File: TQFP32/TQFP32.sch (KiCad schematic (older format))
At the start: 2 parts, among them J1 Conn_01x30, U1 ATmega8L-8AU

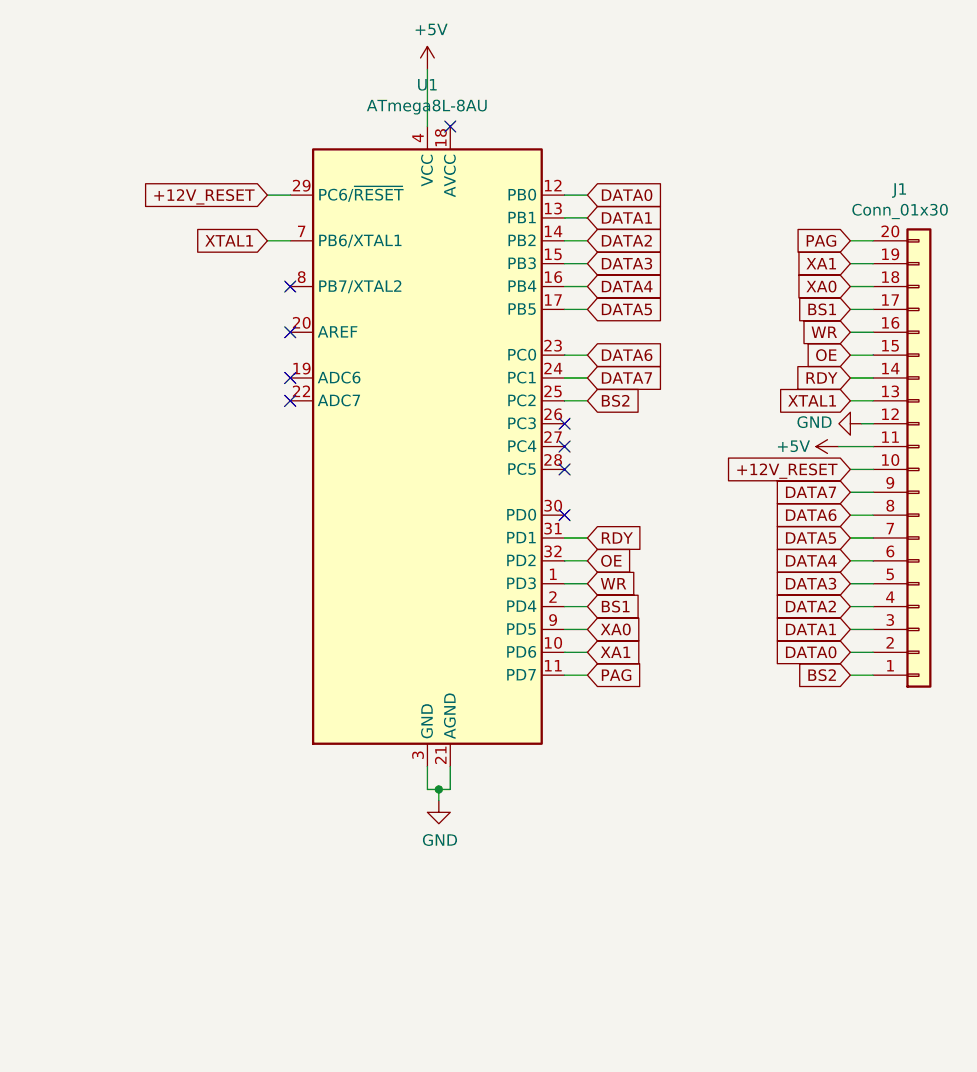
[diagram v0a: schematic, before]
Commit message: Added ISP6 & LED for RESET & LED for POWER
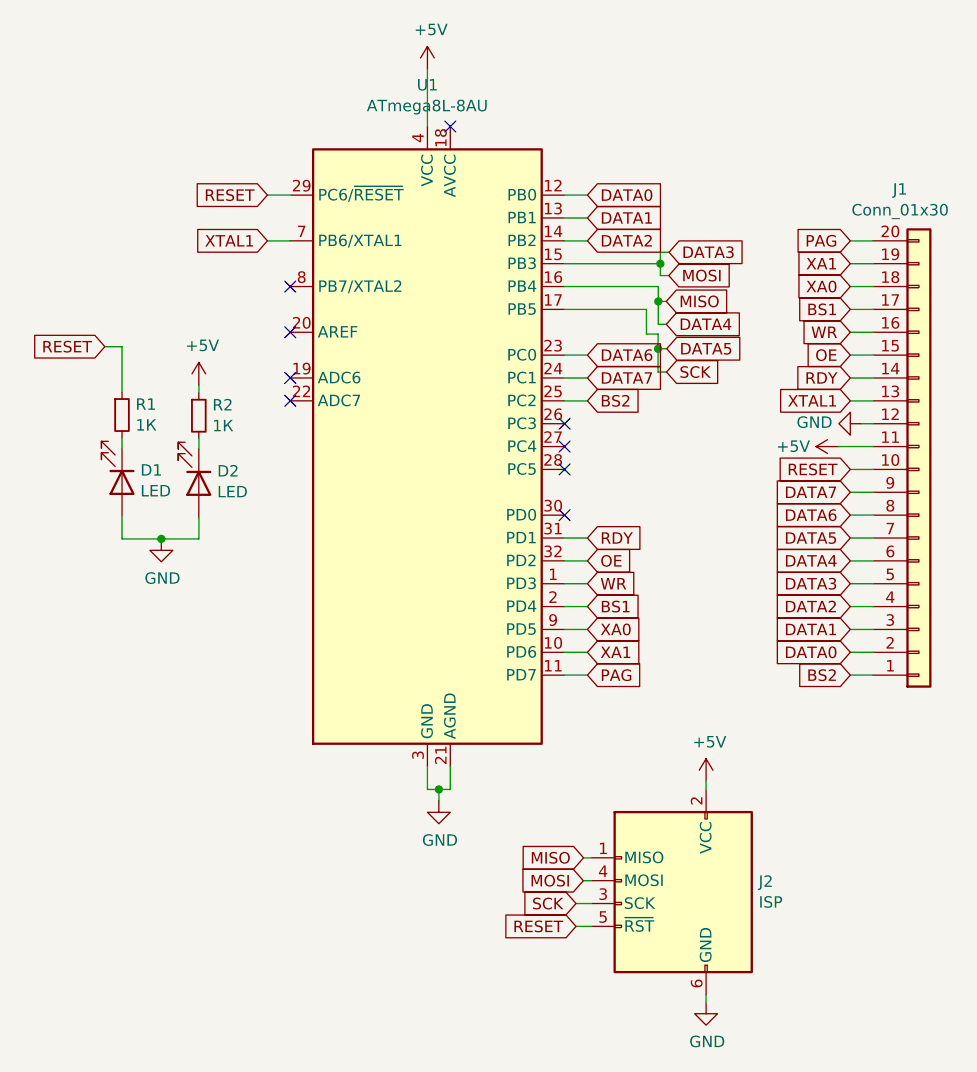
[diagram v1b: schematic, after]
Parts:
- added D1, D2: LED, LED_SMD:LED_0805_2012Metric_Pad1.15x1.40mm_HandSolder, symbol Device:LED
- added J2: ISP, Connector_PinHeader_2.54mm:PinHeader_2x03_P2.54mm_Vertical, symbol Connector:AVR-ISP-6
- added R1, R2: 1К, Resistor_SMD:R_0805_2012Metric_Pad1.20x1.40mm_HandSolder, symbol Device:R_Small
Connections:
- net +5V: now also J2.2 (VCC), R2.1
- net DATA3: now also J2.4 (MOSI)
- net DATA4: now also J2.1 (MISO)
- net DATA5: now also J2.3 (SCK)
- net GND: now also D1.2 (A), D2.2 (A), J2.6 (GND)
- net +12V_RESET renamed RESET
- net RESET: now also J2.5 (~RST), R1.1
- new net: D2.1 (K), R2.2
- new net: D1.1 (K), R1.2
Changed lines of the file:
@@
 $EndDescr
 Text GLabel 4300 2000 0    50   Input ~ 0
-+12V_RESET
+RESET
 Wire Wire Line
 	4300 2000 4400 2000
@@
 Wire Wire Line
 	5700 2100 5600 2100
-Text GLabel 5700 2200 2    50   Input ~ 0
-DATA2
 Wire Wire Line
 	5700 2200 5600 2200
-Wire Wire Line
-	5700 2300 5600 2300
-Text GLabel 5700 2300 2    50   Input ~ 0
-DATA3
-Text GLabel 5700 2400 2    50   Input ~ 0
-DATA4
-Text GLabel 5700 2500 2    50   Input ~ 0
-DATA5
-Wire Wire Line
-	5600 2400 5700 2400
-Wire Wire Line
-	5600 2500 5700 2500
 Text GLabel 5700 2700 2    50   Input ~ 0
 DATA6
@@
 	6950 2200 6850 2200
 Text GLabel 6850 3200 0    50   Input ~ 0
-+12V_RESET
+RESET
 Wire Wire Line
 	6850 3200 6950 3200
@@
 Wire Wire Line
 	6900 3000 6950 3000
+$Comp
+L Connector:AVR-ISP-6 J2
+U 1 1 60AF4D40
+P 6119 5099
+F 0 "J2" H 5789 5195 50  0000 R CNN
+F 1 "ISP" H 5789 5104 50  0000 R CNN
+F 2 "Connector_PinHeader_2.54mm:PinHeader_2x03_P2.54mm_Vertical" V 5869 5149 50  0001 C CNN
+F 3 " ~" H 4844 4549 50  0001 C CNN
+	1    6119 5099
+	-1   0    0    -1
+$EndComp
+Text GLabel 6045 2565 2    50   Input ~ 0
+DATA4
+Wire Wire Line
+	5600 2400 6010 2400
+Text GLabel 6045 2465 2    50   Input ~ 0
+MISO
+Text GLabel 6056 2352 2    50   Input ~ 0
+MOSI
+Text GLabel 5700 2200 2    50   Input ~ 0
+DATA2
+Wire Wire Line
+	6045 2465 6010 2465
+Wire Wire Line
+	6010 2465 6010 2400
+Wire Wire Line
+	6010 2465 6010 2565
+Wire Wire Line
+	6010 2565 6045 2565
+Connection ~ 6010 2465
+Text GLabel 6057 2250 2    50   Input ~ 0
+DATA3
+Wire Wire Line
+	6019 2300 6019 2250
+Wire Wire Line
+	6019 2250 6057 2250
+Wire Wire Line
+	5600 2300 6019 2300
+Wire Wire Line
+	6056 2352 6019 2352
+Wire Wire Line
+	6019 2352 6019 2300
+Connection ~ 6019 2300
+Text GLabel 6046 2774 2    50   Input ~ 0
+SCK
+Text GLabel 6047 2672 2    50   Input ~ 0
+DATA5
+Wire Wire Line
+	6046 2774 6009 2774
+Wire Wire Line
+	6009 2672 6047 2672
+Wire Wire Line
+	5958 2500 5958 2608
+Wire Wire Line
+	5958 2608 6009 2608
+Wire Wire Line
+	5600 2500 5958 2500
+Wire Wire Line
+	6009 2608 6009 2672
+Connection ~ 6009 2672
+Wire Wire Line
+	6009 2672 6009 2774
+Text GLabel 5683 4899 0    50   Input ~ 0
+MISO
+Text GLabel 5682 4999 0    50   Input ~ 0
+MOSI
+Text GLabel 5650 5099 0    50   Input ~ 0
+SCK
+Wire Wire Line
+	5719 5099 5650 5099
+Wire Wire Line
+	5683 4899 5719 4899
+Wire Wire Line
+	5719 4999 5682 4999
+Text GLabel 5650 5199 0    50   Input ~ 0
+RESET
+Wire Wire Line
+	5719 5199 5650 5199
+$Comp
+L power:GND #PWR0105
+U 1 1 60B56BC6
+P 6219 5531
+F 0 "#PWR0105" H 6219 5281 50  0001 C CNN
+F 1 "GND" H 6224 5358 50  0000 C CNN
+F 2 "" H 6219 5531 50  0001 C CNN
+F 3 "" H 6219 5531 50  0001 C CNN
+	1    6219 5531
+	1    0    0    -1
+$EndComp
+$Comp
+L power:+5V #PWR0106
+U 1 1 60B574EF
+P 6219 4566
+F 0 "#PWR0106" H 6219 4416 50  0001 C CNN
+F 1 "+5V" H 6234 4739 50  0000 C CNN
+F 2 "" H 6219 4566 50  0001 C CNN
+F 3 "" H 6219 4566 50  0001 C CNN
+	1    6219 4566
+	1    0    0    -1
+$EndComp
+Wire Wire Line
+	6219 4566 6219 4599
+Wire Wire Line
+	6219 5531 6219 5499
+$Comp
+L Device:LED D2
+U 1 1 60B87E9D
+P 4000 3261
+F 0 "D2" V 3947 3341 50  0000 L CNN
+F 1 "LED" V 4038 3341 50  0000 L CNN
+F 2 "LED_SMD:LED_0805_2012Metric_Pad1.15x1.40mm_HandSolder" H 4000 3261 50  0001 C CNN
+F 3 "~" H 4000 3261 50  0001 C CNN
+	1    4000 3261
+	0    1    1    0
+$EndComp
+$Comp
+L Device:LED D1
+U 1 1 60B8D8E2
+P 3664 3257
+F 0 "D1" V 3611 3337 50  0000 L CNN
+F 1 "LED" V 3702 3337 50  0000 L CNN
+F 2 "LED_SMD:LED_0805_2012Metric_Pad1.15x1.40mm_HandSolder" H 3664 3257 50  0001 C CNN
+F 3 "~" H 3664 3257 50  0001 C CNN
+	1    3664 3257
+	0    1    1    0
+$EndComp
+$Comp
+L power:GND #PWR0107
+U 1 1 60B93CD4
+P 3836 3504
+F 0 "#PWR0107" H 3836 3254 50  0001 C CNN
+F 1 "GND" H 3841 3331 50  0000 C CNN
+F 2 "" H 3836 3504 50  0001 C CNN
+F 3 "" H 3836 3504 50  0001 C CNN
+	1    3836 3504
+	1    0    0    -1
+$EndComp
+Wire Wire Line
+	3664 3407 3664 3504
+Wire Wire Line
+	3664 3504 3836 3504
+Wire Wire Line
+	3836 3504 4000 3504
+Wire Wire Line
+	4000 3504 4000 3411
+Connection ~ 3836 3504
+Text GLabel 3589 2663 0    50   Input ~ 0
+RESET
+$Comp
+L Device:R_Small R2
+U 1 1 60BA6720
+P 4000 2965
+F 0 "R2" H 4059 3011 50  0000 L CNN
+F 1 "1К" H 4059 2920 50  0000 L CNN
+F 2 "Resistor_SMD:R_0805_2012Metric_Pad1.20x1.40mm_HandSolder" H 4000 2965 50  0001 C CNN
+F 3 "~" H 4000 2965 50  0001 C CNN
+	1    4000 2965
+	1    0    0    -1
+$EndComp
+$Comp
+L Device:R_Small R1
+U 1 1 60BA4C2B
+P 3664 2962
+F 0 "R1" H 3723 3008 50  0000 L CNN
+F 1 "1К" H 3723 2917 50  0000 L CNN
+F 2 "Resistor_SMD:R_0805_2012Metric_Pad1.20x1.40mm_HandSolder" H 3664 2962 50  0001 C CNN
+F 3 "~" H 3664 2962 50  0001 C CNN
+	1    3664 2962
+	1    0    0    -1
+$EndComp
+Wire Wire Line
+	3664 3107 3664 3062
+Wire Wire Line
+	4000 3065 4000 3111
+Wire Wire Line
+	3664 2862 3664 2663
+Wire Wire Line
+	3664 2663 3589 2663
+$Comp
+L power:+5V #PWR0108
+U 1 1 60BBC980
+P 4000 2832
+F 0 "#PWR0108" H 4000 2682 50  0001 C CNN
+F 1 "+5V" H 4015 3005 50  0000 C CNN
+F 2 "" H 4000 2832 50  0001 C CNN
+F 3 "" H 4000 2832 50  0001 C CNN
+	1    4000 2832
+	1    0    0    -1
+$EndComp
+Wire Wire Line
+	4000 2865 4000 2832
 $EndSCHEMATC
